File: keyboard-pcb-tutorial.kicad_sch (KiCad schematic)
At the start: 14 parts

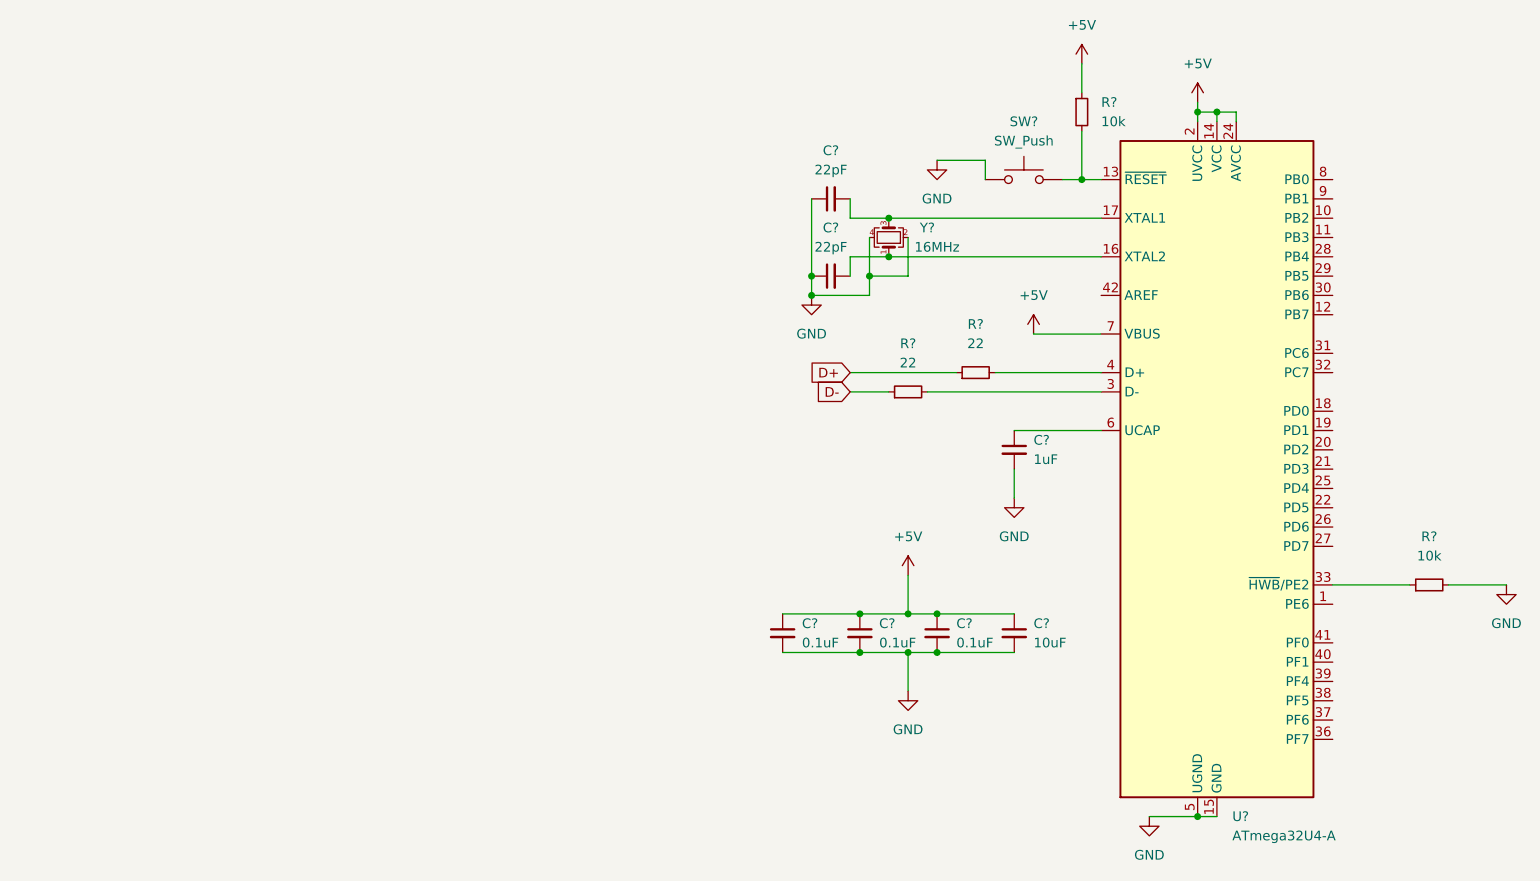
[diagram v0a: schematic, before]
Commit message: Added footprint bindings
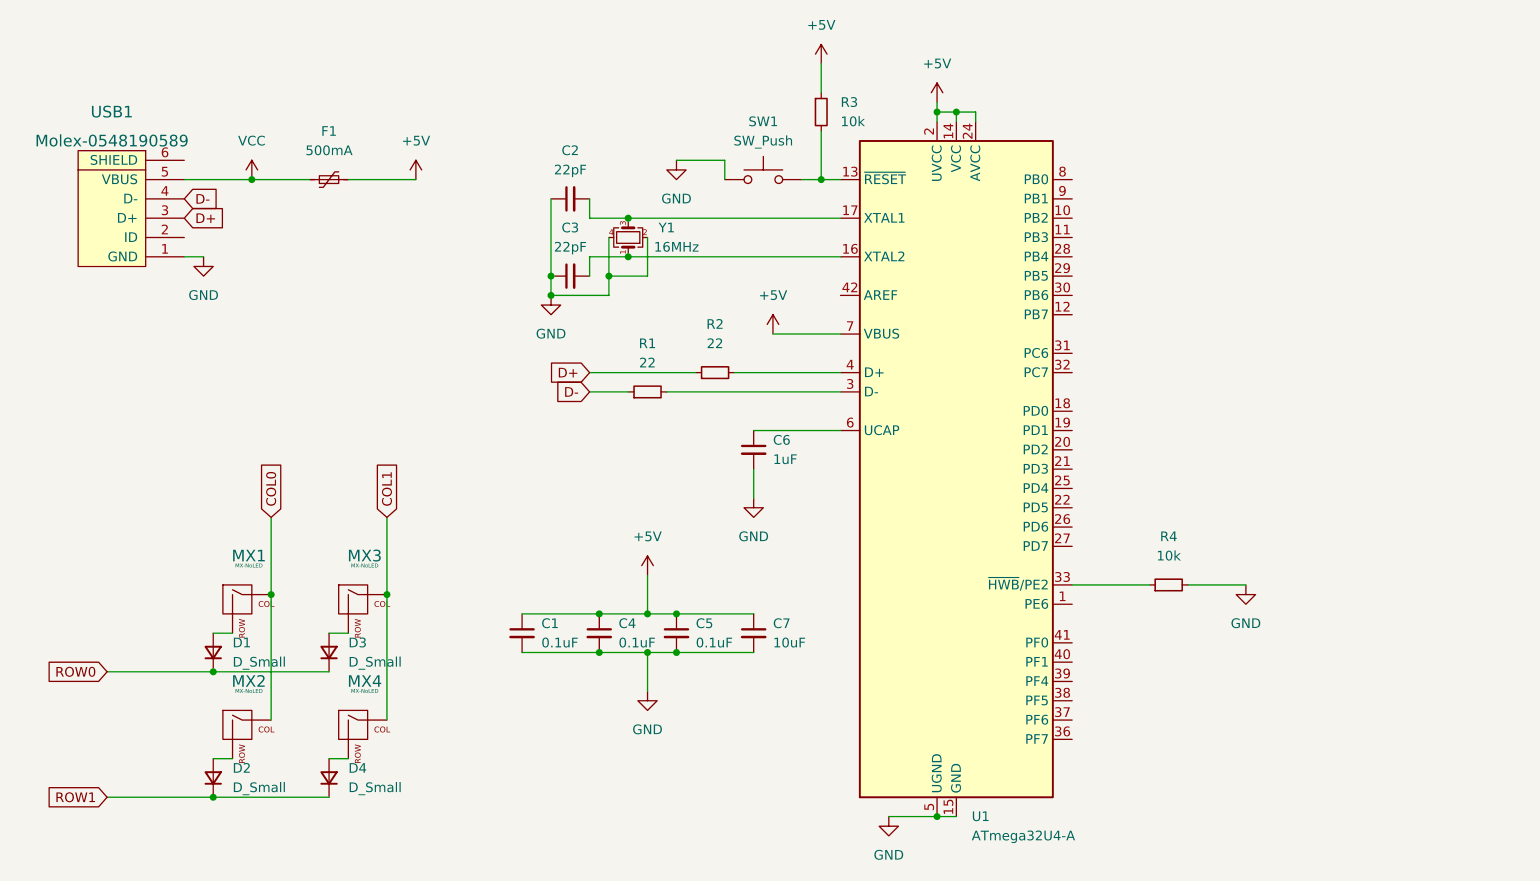
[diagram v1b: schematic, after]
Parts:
- added D1, D2, D3, D4: D_Small, Diode_SMD:D_SOD-123, symbol Device:D_Small
- added F1: 500mA, Fuse:Fuse_1206_3216Metric, symbol Device:Polyfuse_Small
- added MX1, MX2, MX3, MX4: MX-NoLED, MX_Alps_Hybrid:MX-1U-NoLED, symbol MX_Alps_Hybrid:MX-NoLED
- added USB1: Molex-0548190589, random-keyboard-parts:Molex-0548190589, symbol random-keyboard-parts:Molex-0548190589
- C1, C2, C3, C4, C5, C6, C7: renamed from C?; footprint (none) -> Capacitor_SMD:C_0805_2012Metric
- R1, R2, R3, R4: renamed from R?; footprint (none) -> Resistor_SMD:R_0805_2012Metric
- SW1: renamed from SW?; footprint (none) -> random-keyboard-parts:SKQG-1155865
- Y1: renamed from Y?; footprint (none) -> Crystal:Crystal_SMD_3225-4Pin_3.2x2.5mm
- gave numbers to parts that had none: 1
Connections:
- net +5V: now also F1.2
- net D+: now also USB1.3 (D+)
- net D-: now also USB1.4 (D-)
- net GND: now also USB1.1 (GND)
- new net: D2.2 (A), MX2.2 (ROW)
- new net: D3.2 (A), MX3.2 (ROW)
- new net: D1.2 (A), MX1.2 (ROW)
- new net: D4.2 (A), MX4.2 (ROW)
- new net COL0: MX1.1 (COL), MX2.1 (COL)
- new net COL1: MX3.1 (COL), MX4.1 (COL)
- new net ROW0: D1.1 (K), D3.1 (K)
- new net ROW1: D2.1 (K), D4.1 (K)
- new net VCC: F1.1, USB1.5 (VBUS)
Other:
- moved on the sheet: C1, C2, C3, C4, C5, C6, C7, R1, R2, R3, R4, SW1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

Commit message: Added routing
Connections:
- net COL0: now also U1.29 (PB5)
- net COL1: now also U1.28 (PB4)
- net ROW0: now also U1.27 (PD7)
- net ROW1: now also U1.30 (PB6)
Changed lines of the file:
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@@
     (stroke (width 0) (type default) (color 0 0 0 0))
+  )
+  (global_label "COL1" (shape input) (at 209.55 60.96 0) (fields_autoplaced)
+    (effects (font (size 1.27 1.27)) (justify left))
+    (property "Intersheet References" "${INTERSHEET_REFS}" (id 0) (at 216.8012 60.8806 0)
+      (effects (font (size 1.27 1.27)) (justify left) hide)
+    )
   )
   (global_label "ROW1" (shape input) (at 82.55 132.08 180) (fields_autoplaced)
@@
     )
   )
+  (global_label "COL0" (shape input) (at 209.55 63.5 0) (fields_autoplaced)
+    (effects (font (size 1.27 1.27)) (justify left))
+    (property "Intersheet References" "${INTERSHEET_REFS}" (id 0) (at 216.8012 63.4206 0)
+      (effects (font (size 1.27 1.27)) (justify left) hide)
+    )
+  )
+  (global_label "ROW1" (shape input) (at 209.55 66.04 0) (fields_autoplaced)
+    (effects (font (size 1.27 1.27)) (justify left))
+    (property "Intersheet References" "${INTERSHEET_REFS}" (id 0) (at 217.2245 65.9606 0)
+      (effects (font (size 1.27 1.27)) (justify left) hide)
+    )
+  )
   (global_label "ROW0" (shape input) (at 82.55 115.57 180) (fields_autoplaced)
     (effects (font (size 1.27 1.27)) (justify right))
@@
       (effects (font (size 1.27 1.27)) (justify left) hide)
     )
+  )
+  (global_label "ROW0" (shape input) (at 209.55 99.06 0) (fields_autoplaced)
+    (effects (font (size 1.27 1.27)) (justify left))
+    (property "Intersheet References" "${INTERSHEET_REFS}" (id 0) (at 217.2245 98.9806 0)
+      (effects (font (size 1.27 1.27)) (justify left) hide)
+    )
